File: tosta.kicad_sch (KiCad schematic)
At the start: 26 parts, among them J1 UEXT, Q1 MMBT3904, SW1 SW_Push, SW2 SW_Push, SW3 SW_Push, SW4 SW_Push, U1 STM32G030KxT, U2 LPH7366

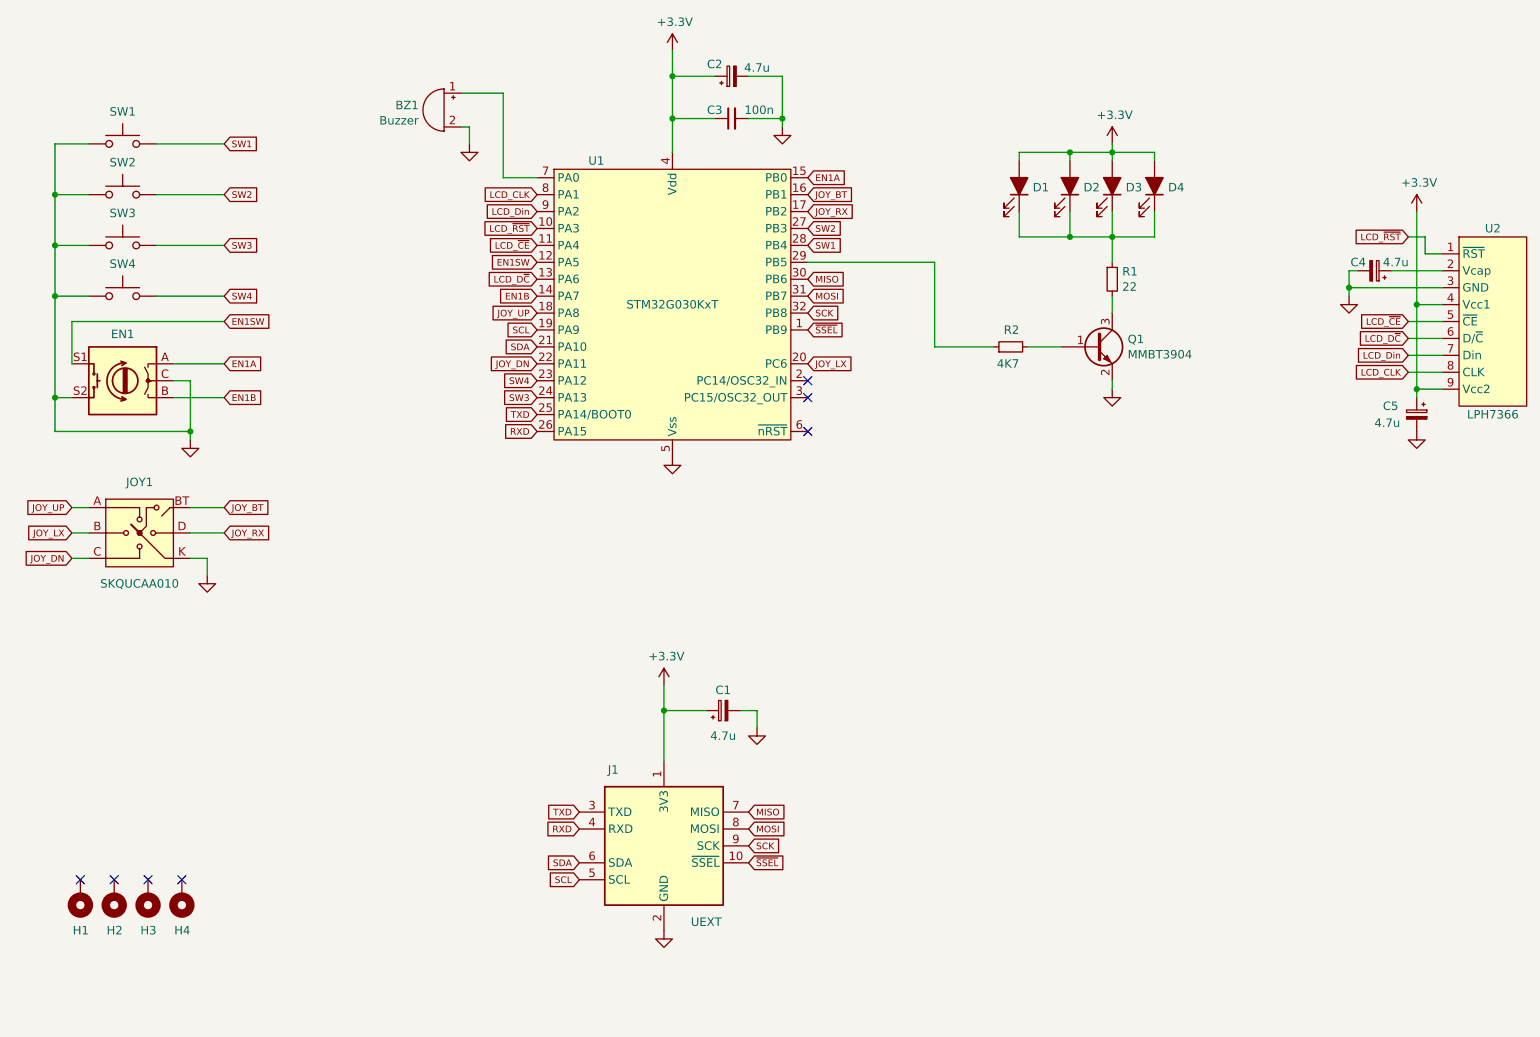
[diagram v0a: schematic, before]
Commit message: Added SWD header
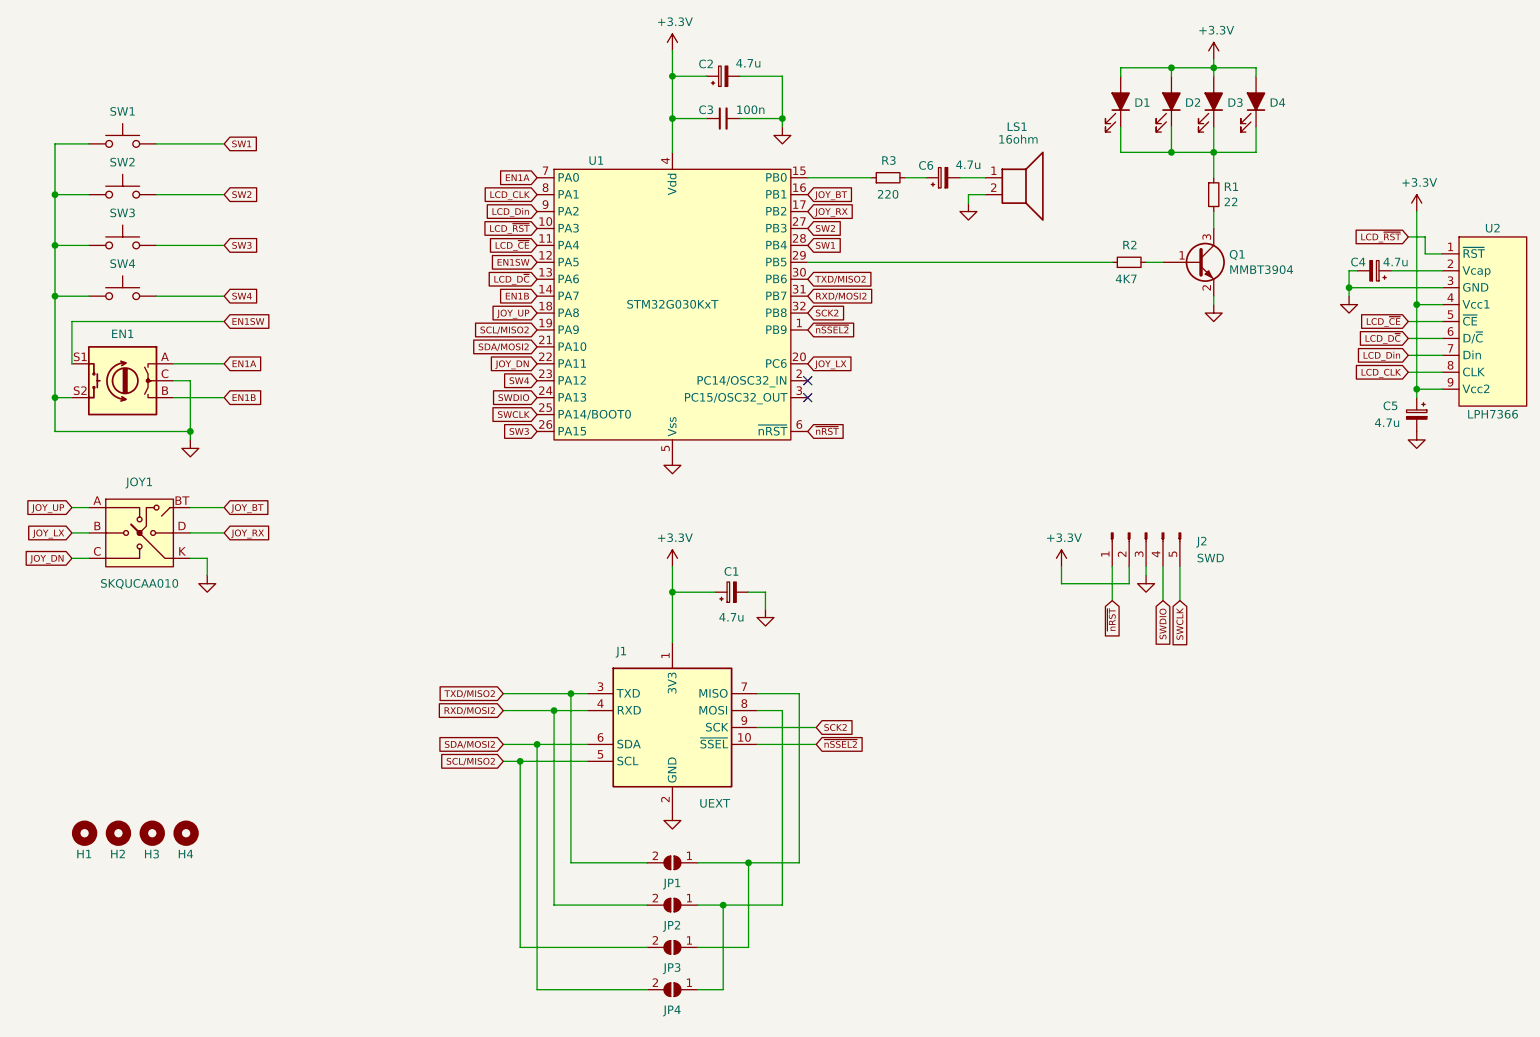
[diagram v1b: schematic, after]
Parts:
- removed BZ1: Buzzer, Tosta:KY_BUZ, symbol Device:Buzzer
- removed H1, H2, H3, H4: MountingHole_Pad, Tosta:M3_ISO7380, symbol Mechanical:MountingHole_Pad
- added C6: 4.7u, Capacitor_Tantalum_SMD:CP_EIA-3216-12_Kemet-S_Pad1.58x1.35mm_HandSolder, symbol Device:CP_Small
- added H1, H2, H3, H4: MountingHole, Tosta:M3_ISO7380, symbol Mechanical:MountingHole
- added J2: SWD, Connector_PinHeader_2.54mm:PinHeader_1x05_P2.54mm_Vertical, symbol Connector:Conn_01x05_Male
- added JP1, JP2, JP3, JP4: SolderJumper_2_Open, Jumper:SolderJumper-2_P1.3mm_Open_RoundedPad1.0x1.5mm, symbol Jumper:SolderJumper_2_Open
- added LS1: 16ohm, Tosta:KY_BUZ, symbol Device:Speaker
- added R3: 220, Resistor_SMD:R_0805_2012Metric_Pad1.20x1.40mm_HandSolder, symbol Device:R_Small
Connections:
- net +3V3: now also J2.2 (Pin_2)
- net EN1A: now also U1.7 (PA0); no longer U1.15 (PB0)
- net GND: now also J2.3 (Pin_3), LS1.2
- net SW3: now also U1.26 (PA15); no longer U1.24 (PA13)
- net ~nRST: now reaches U1.6 (~nRST)
- net ~nRST: now also J2.1 (Pin_1)
- net MISO: no longer names the net of J1.7 (MISO)
- net MISO: now also JP1.1 (A), JP3.1 (A); no longer U1.30 (PB6)
- net MOSI: no longer names the net of J1.8 (MOSI)
- net MOSI: now also JP2.1 (A), JP4.1 (A); no longer U1.31 (PB7)
- net RXD renamed RXD/MOSI2
- net RXD/MOSI2: now also U1.31 (PB7), JP2.2 (B); no longer U1.26 (PA15)
- net SCK renamed SCK2
- net SCL renamed SCL/MISO2
- net SCL/MISO2: now also JP3.2 (B)
- net SDA renamed SDA/MOSI2
- net SDA/MOSI2: now also JP4.2 (B)
- net TXD renamed SWCLK
- net SWCLK: now also J2.5 (Pin_5); no longer J1.3 (TXD)
- net ~SSEL renamed ~nSSEL2
- new net: R3.1, U1.15 (PB0)
- new net: C6.1, R3.2
- new net: C6.2, LS1.1
- new net SWDIO: J2.4 (Pin_4), U1.24 (PA13)
- new net TXD/MISO2: J1.3 (TXD), JP1.2 (B), U1.30 (PB6)
- no-connect marks 7 -> 2
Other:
- moved on the sheet: C1, C2, C3, D1, D2, D3, D4, J1, Q1, R1, R2

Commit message: Updated speaker driver
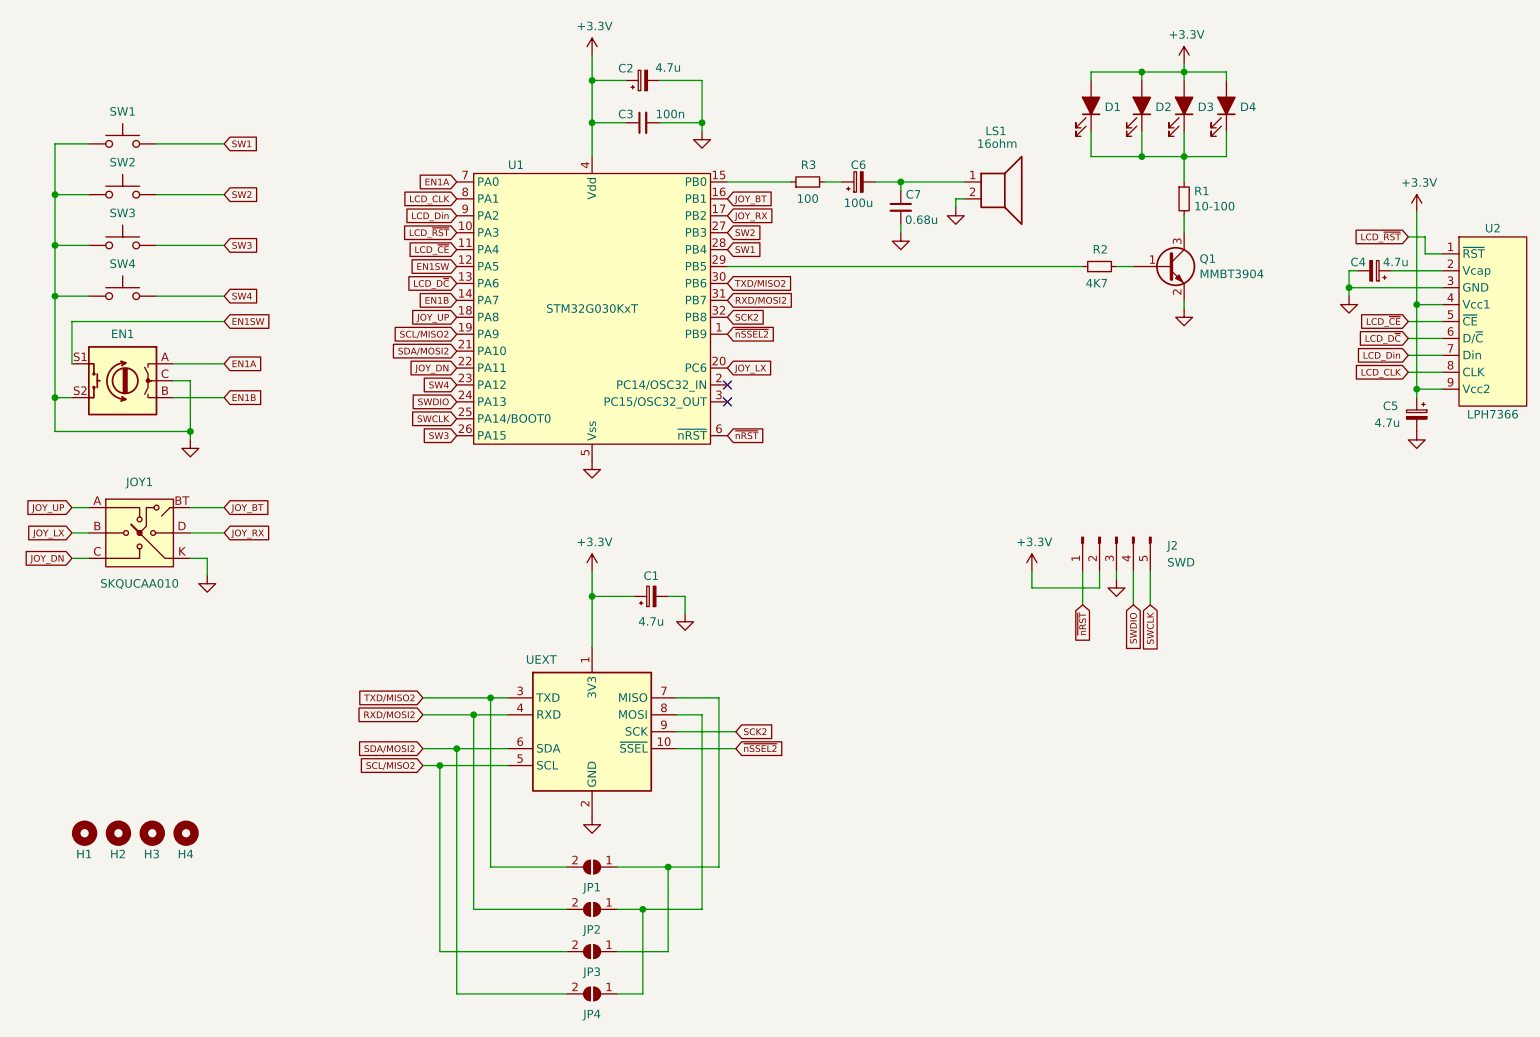
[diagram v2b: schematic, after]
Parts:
- added C7: 0.68u, Capacitor_SMD:C_0805_2012Metric_Pad1.18x1.45mm_HandSolder, symbol Device:C_Small
- C6: value 4.7u -> 100u
- R1: value 22 -> 10-100
- R3: value 220 -> 100
- renumbered J1 to UEXT
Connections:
- net GND: now also C7.2
- net at C6.2, LS1.1: now also C7.1
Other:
- moved on the sheet: C1, C2, C3, C6, D1, D2, D3, D4, J2, JP1, JP2, JP3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
